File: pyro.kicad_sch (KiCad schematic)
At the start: 35 parts, among them J2 PYRO_1, J3 PYRO_2, J4 PYRO_3, J5 PYRO_4, Q0 BJT - NPN, Q1 PMOS, Q2 PMOS, Q3 PMOS, Q4 PMOS, Q5 NMOS, Q6 NMOS, Q7 NMOS, Q8 NMOS, Q9 NMOS

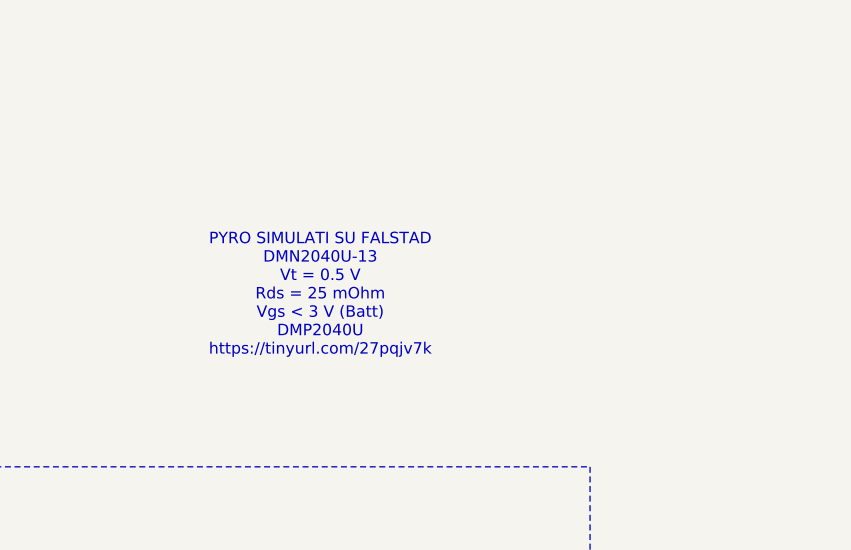
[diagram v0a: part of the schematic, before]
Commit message: update blocco pyro
scelta pmos e bjt
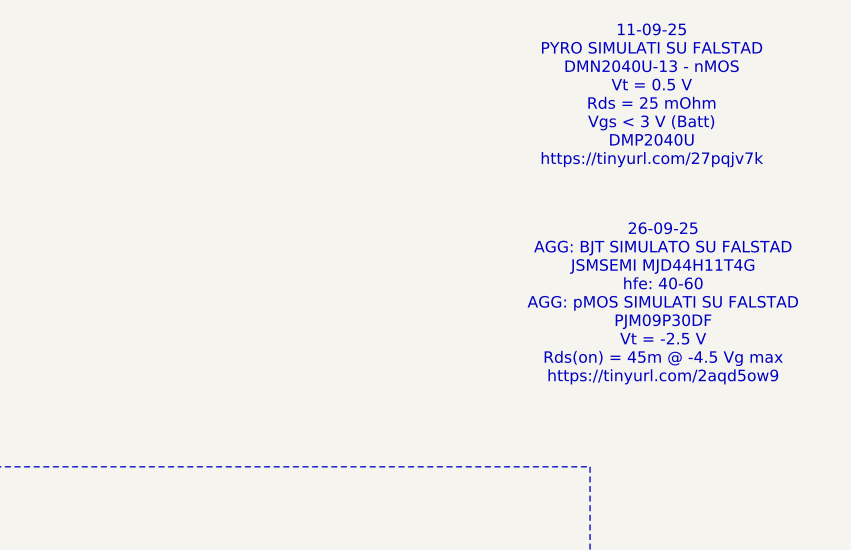
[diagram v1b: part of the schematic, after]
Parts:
- Q5, Q6, Q7, Q8, Q9: footprint (none) -> Package_TO_SOT_SMD:SOT-23_Handsoldering
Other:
- note added: "11-09-25 PYRO SIMULATI SU FALSTAD DMN2040U-13 - nMOS Vt = 0.5 V Rds = 25 mOhm Vgs < 3 V (Batt) DMP2040U https://tinyurl.com/27pqjv7k"
- note added: "26-09-25 AGG: BJT SIMULATO SU FALSTAD JSMSEMI MJD44H11T4G hfe: 40-60 AGG: pMOS SIMULATI SU FALSTAD PJM09P30DF Vt = -2.5 V Rds(on) = 45m @ -4.5 Vg max https://tinyurl.com/2aqd5ow9"
- note removed: "PYRO SIMULATI SU FALSTAD DMN2040U-13 Vt = 0.5 V Rds = 25 mOhm Vgs < 3 V (Batt) DMP2040U https://tinyurl.com/27pqjv7k"
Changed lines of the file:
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@@
 		)
 	)
-	(text "PYRO SIMULATI SU FALSTAD\nDMN2040U-13\nVt = 0.5 V\nRds = 25 mOhm\nVgs < 3 V (Batt)\nDMP2040U\nhttps://tinyurl.com/27pqjv7k"
+	(text "11-09-25\nPYRO SIMULATI SU FALSTAD\nDMN2040U-13 - nMOS\nVt = 0.5 V\nRds = 25 mOhm\nVgs < 3 V (Batt)\nDMP2040U\nhttps://tinyurl.com/27pqjv7k"
 		(exclude_from_sim no)
-		(at 217.678 45.72 0)
+		(at 254.508 23.622 0)
 		(effects
 			(font
@@
 		)
 	)
+	(text "26-09-25\nAGG: BJT SIMULATO SU FALSTAD\nJSMSEMI MJD44H11T4G\nhfe: 40-60\nAGG: pMOS SIMULATI SU FALSTAD\nPJM09P30DF\nVt = -2.5 V\nRds(on) = 45m @ -4.5 Vg max\nhttps://tinyurl.com/2aqd5ow9"
+		(exclude_from_sim no)
+		(at 255.778 46.736 0)
+		(effects
+			(font
+				(size 1.27 1.27)
+			)
+		)
+	)
 	(text "9"
 		(exclude_from_sim no)
@@
 			)
 		)
-		(property "Footprint" ""
+		(property "Footprint" "Package_TO_SOT_SMD:SOT-23_Handsoldering"
 			(at 76.2 88.9 0)
 			(effects
@@
 			)
 		)
-		(property "Footprint" ""
+		(property "Footprint" "Package_TO_SOT_SMD:SOT-23_Handsoldering"
 			(at 170.18 88.9 0)
 			(effects
@@
 			)
 		)
-		(property "Footprint" ""
+		(property "Footprint" "Package_TO_SOT_SMD:SOT-23_Handsoldering"
 			(at 123.19 88.9 0)
 			(effects
@@
 			)
 		)
-		(property "Footprint" ""
+		(property "Footprint" "Package_TO_SOT_SMD:SOT-23_Handsoldering"
 			(at 217.17 88.9 0)
 			(effects
@@
 			)
 		)
-		(property "Footprint" ""
+		(property "Footprint" "Package_TO_SOT_SMD:SOT-23_Handsoldering"
 			(at 151.13 135.89 0)
 			(effects

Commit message: bozza layout pcb
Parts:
- removed J2: PYRO_1, symbol Connector:Conn_01x02_Socket
- removed J3: PYRO_2, symbol Connector:Conn_01x02_Socket
- removed J4: PYRO_3, symbol Connector:Conn_01x02_Socket
- removed J5: PYRO_4, symbol Connector:Conn_01x02_Socket
- removed Q0: BJT - NPN, symbol Transistor_BJT:Q_NPN_BCE
- removed Q1, Q2, Q3, Q4: PMOS, symbol Simulation_SPICE:PMOS
- added J15: DB141R-2.54-8P-GN, DB141R-2-54-8:CONN16_DB141R_DIO, symbol 2025-09-27_12-32-40:DB141R-2.54-8P-GN
- added Q1: MJD44H11T4G, easyeda2kicad:TO-252-2_L6.5-W6.1-P4.58-LS10.0-TL, symbol WF5803F:MJD44H11T4G
- added Q10, Q11, Q12, Q13: PJM09P30DF, easyeda2kicad:DFN-6_L2.0-W2.0-P0.65-BL-EP-1, symbol WF5803F:PJM09P30DF
- added R9: 100, Resistor_SMD:R_0603_1608Metric_Pad0.98x0.95mm_HandSolder, symbol Device:R
- added U6: LT3092xST, Package_TO_SOT_SMD:SOT-223-3_TabPin2, symbol Reference_Current:LT3092xST
- R8: value 500 -> 200k
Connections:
- net +BATT: now also Q1.4 (C), U6.3; no longer R8.1
- net PYRO_HIGH: now also Q1.3 (E), Q10.4 (S), Q11.4 (S), Q12.4 (S), Q13.4 (S)
- net PYRO_LOW: now also J15.10, J15.12, J15.14, J15.16, J15.2, J15.4, J15.6, J15.8
- net at R15.2, R16.1: now also Q11.3 (G)
- net at R17.2, R34.1: now also Q12.3 (G)
- net at R12.2, R14.1: now also Q10.3 (G)
- net at R37.2, R38.1: now also Q13.3 (G)
- net at R8.2: now also Q1.1 (B), R9.2
- new net: R8.1, U6.1
- new net: R9.1, U6.2
- new net PYRO1: J15.1, J15.9, Q10.1 (D)
- new net PYRO2: J15.11, J15.3, Q11.1 (D)
- new net PYRO3: J15.13, J15.5, Q12.1 (D)
- new net PYRO4: J15.15, J15.7, Q13.1 (D)
- no-connect marks 0 -> 20
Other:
- note added: "27-09-25 AGG: GENERATORE DI CORRENTE LT3092 Iout = 20 mA Rout = 100 Ohm Rset = 200k Ohm https://tinyurl.com/2dp3mgog + aggiornamento beta pMOS beta = 2.27 https://tinyurl.com/2dp3mgog"

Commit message: led e buzzer
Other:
- moved on the sheet: J15
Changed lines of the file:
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@@
 	)
 	(junction
-		(at 78.74 173.99)
+		(at 64.77 153.67)
 		(diameter 0)
 		(color 0 0 0 0)
@@
 	)
 	(junction
-		(at 78.74 168.91)
+		(at 64.77 148.59)
 		(diameter 0)
 		(color 0 0 0 0)
@@
 	)
 	(junction
-		(at 78.74 179.07)
+		(at 64.77 158.75)
 		(diameter 0)
 		(color 0 0 0 0)
 	)
 	(junction
-		(at 78.74 158.75)
+		(at 64.77 138.43)
 		(diameter 0)
 		(color 0 0 0 0)
@@
 	)
 	(junction
-		(at 78.74 184.15)
+		(at 64.77 163.83)
 		(diameter 0)
 		(color 0 0 0 0)
 	)
 	(junction
-		(at 78.74 153.67)
+		(at 64.77 133.35)
 		(diameter 0)
 		(color 0 0 0 0)
@@
 	)
 	(junction
-		(at 78.74 148.59)
+		(at 64.77 128.27)
 		(diameter 0)
 		(color 0 0 0 0)
 	)
 	(junction
-		(at 78.74 163.83)
+		(at 64.77 143.51)
 		(diameter 0)
 		(color 0 0 0 0)
@@
 	(wire
 		(pts
-			(xy 78.74 173.99) (xy 78.74 176.53)
-		)
-		(stroke
-			(width 0)
-			(type default)
-		)
-	)
-	(wire
-		(pts
-			(xy 78.74 163.83) (xy 78.74 166.37)
+			(xy 64.77 153.67) (xy 64.77 156.21)
+		)
+		(stroke
+			(width 0)
+			(type default)
+		)
+	)
+	(wire
+		(pts
+			(xy 64.77 143.51) (xy 64.77 146.05)
 		)
 		(stroke
@@
 	(wire
 		(pts
-			(xy 78.74 148.59) (xy 78.74 151.13)
+			(xy 64.77 128.27) (xy 64.77 130.81)
 		)
 		(stroke
@@
 	(wire
 		(pts
-			(xy 78.74 184.15) (xy 78.74 186.69)
+			(xy 64.77 163.83) (xy 64.77 166.37)
 		)
 		(stroke
@@
 	(wire
 		(pts
-			(xy 68.58 153.67) (xy 78.74 153.67)
+			(xy 54.61 133.35) (xy 64.77 133.35)
 		)
 		(stroke
@@
 	(wire
 		(pts
-			(xy 68.58 173.99) (xy 78.74 173.99)
+			(xy 54.61 153.67) (xy 64.77 153.67)
 		)
 		(stroke
@@
 	(wire
 		(pts
-			(xy 78.74 153.67) (xy 78.74 156.21)
-		)
-		(stroke
-			(width 0)
-			(type default)
-		)
-	)
-	(wire
-		(pts
-			(xy 68.58 168.91) (xy 78.74 168.91)
+			(xy 64.77 133.35) (xy 64.77 135.89)
+		)
+		(stroke
+			(width 0)
+			(type default)
+		)
+	)
+	(wire
+		(pts
+			(xy 54.61 148.59) (xy 64.77 148.59)
 		)
 		(stroke
@@
 	(wire
 		(pts
-			(xy 78.74 158.75) (xy 78.74 161.29)
+			(xy 64.77 138.43) (xy 64.77 140.97)
 		)
 		(stroke
@@
 	(wire
 		(pts
-			(xy 68.58 158.75) (xy 78.74 158.75)
-		)
-		(stroke
-			(width 0)
-			(type default)
-		)
-	)
-	(wire
-		(pts
-			(xy 68.58 163.83) (xy 78.74 163.83)
+			(xy 54.61 138.43) (xy 64.77 138.43)
+		)
+		(stroke
+			(width 0)
+			(type default)
+		)
+	)
+	(wire
+		(pts
+			(xy 54.61 143.51) (xy 64.77 143.51)
 		)
 		(stroke
@@
 	(wire
 		(pts
-			(xy 68.58 184.15) (xy 78.74 184.15)
+			(xy 54.61 163.83) (xy 64.77 163.83)
 		)
 		(stroke
@@
 	(wire
 		(pts
-			(xy 68.58 179.07) (xy 78.74 179.07)
+			(xy 54.61 158.75) (xy 64.77 158.75)
 		)
 		(stroke
@@
 	(wire
 		(pts
-			(xy 78.74 179.07) (xy 78.74 181.61)
+			(xy 64.77 158.75) (xy 64.77 161.29)
 		)
 		(stroke
@@
 	(wire
 		(pts
-			(xy 68.58 148.59) (xy 78.74 148.59)
-		)
-		(stroke
-			(width 0)
-			(type default)
-		)
-	)
-	(wire
-		(pts
-			(xy 78.74 168.91) (xy 78.74 171.45)
+			(xy 54.61 128.27) (xy 64.77 128.27)
+		)
+		(stroke
+			(width 0)
+			(type default)
+		)
+	)
+	(wire
+		(pts
+			(xy 64.77 148.59) (xy 64.77 151.13)
 		)
 		(stroke
@@
 	)
 	(label "PYRO_LOW"
-		(at 68.58 173.99 180)
+		(at 54.61 153.67 180)
 		(effects
 			(font
@@
 	)
 	(label "PYRO_LOW"
-		(at 68.58 163.83 180)
+		(at 54.61 143.51 180)
 		(effects
 			(font
@@
 	)
 	(label "PYRO2"
-		(at 68.58 158.75 180)
+		(at 54.61 138.43 180)
 		(effects
 			(font
@@
 	)
 	(label "PYRO3"
-		(at 68.58 168.91 180)
+		(at 54.61 148.59 180)
 		(effects
 			(font
@@
 	)
 	(label "PYRO4"
-		(at 68.58 179.07 180)
+		(at 54.61 158.75 180)
 		(effects
 			(font
@@
 	)
 	(label "PYRO_LOW"
-		(at 68.58 184.15 180)
+		(at 54.61 163.83 180)
 		(effects
 			(font
@@
 	)
 	(label "PYRO_LOW"
-		(at 68.58 153.67 180)
+		(at 54.61 133.35 180)
 		(effects
 			(font
@@
 	)
 	(label "PYRO1"
-		(at 68.58 148.59 180)
+		(at 54.61 128.27 180)
 		(effects
 			(font
@@
 	(symbol
 		(lib_id "2025-09-27_12-32-40:DB141R-2.54-8P-GN")
-		(at 78.74 148.59 0)
+		(at 64.77 128.27 0)
 		(unit 1)
 		(exclude_from_sim no)
@@
 		(fields_autoplaced yes)
 		(property "Reference" "J15"
-			(at 92.71 166.3699 0)
+			(at 78.74 146.0499 0)
 			(effects
 				(font
@@
 		)
 		(property "Value" "DB141R-2.54-8P-GN"
-			(at 92.71 168.9099 0)
+			(at 78.74 148.5899 0)
 			(effects
 				(font
@@
 		)
 		(property "Footprint" "DB141R-2-54-8:CONN16_DB141R_DIO"
-			(at 78.74 148.59 0)
+			(at 64.77 128.27 0)
 			(effects
 				(font
@@
 		)
 		(property "Datasheet" "DB141R-2.54-8P-GN"
-			(at 78.74 148.59 0)
+			(at 64.77 128.27 0)
 			(effects
 				(font
@@
 		)
 		(property "Description" ""
-			(at 78.74 148.59 0)
-			(effects
-				(font
+			(at 64.77 128.27 0)
+			(effects
+				(font

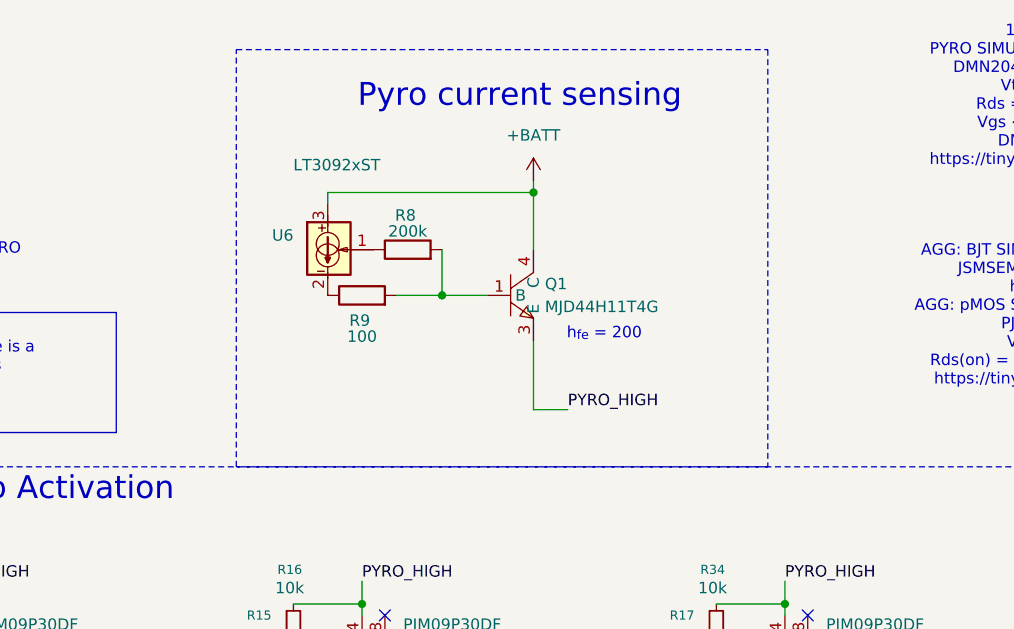
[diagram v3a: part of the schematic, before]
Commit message: Small changes
modified Main LEDs.
Added Radio LEDs.

Connected the GPS uart to the Radio.
Added a test point for the GPS PRG pin.

Modified the Pyro current limiter for better BOM compliance.

Modified a copule of estetic things on the schematic.
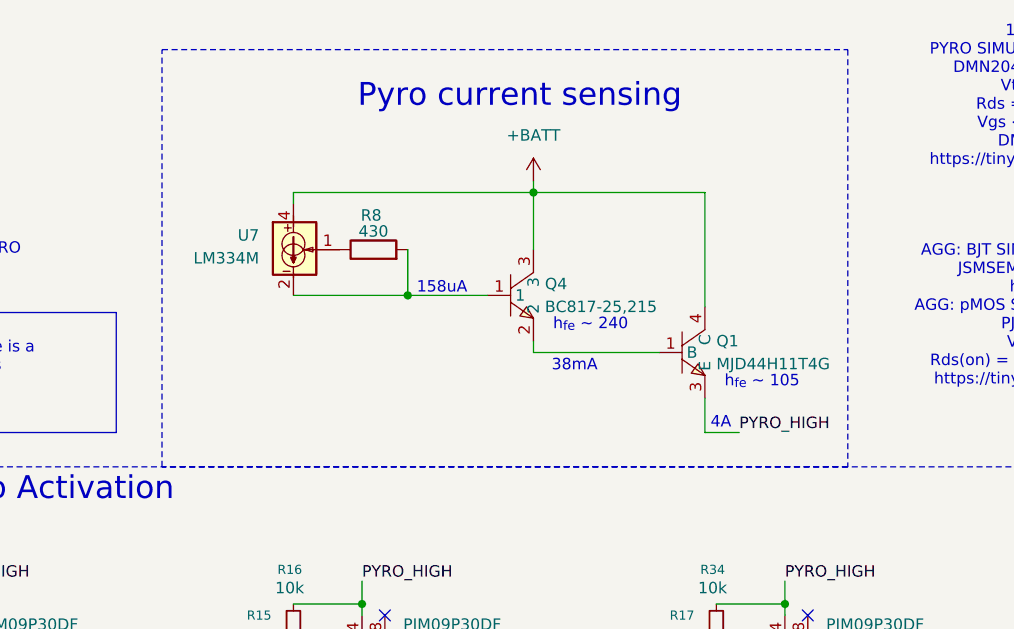
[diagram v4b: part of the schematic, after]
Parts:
- removed R9: 100, Resistor_SMD:R_0603_1608Metric_Pad0.98x0.95mm_HandSolder, symbol Device:R
- removed U6: LT3092xST, Package_TO_SOT_SMD:SOT-223-3_TabPin2, symbol Reference_Current:LT3092xST
- added Q4: BC817-25,215, BC817-25:SOT-23-3_L2.9-W1.6-P1.90-LS2.8-BR, symbol BC817-25:BC817-25,215
- added U7: LM334M, Package_SO:SOIC-8_3.9x4.9mm_P1.27mm, symbol Reference_Current:LM334M
- R8: value 200k -> 430
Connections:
- net +BATT: now also Q4.3, U7.4
- net at R8.1: now also U7.1
- net at R8.2: now also Q4.1, U7.2, U7.3, U7.6, U7.7; no longer Q1.1 (B)
- new net: Q1.1 (B), Q4.2
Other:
- note added: "158uA"
- note added: "38mA"
- note added: "4A"
- note added: "h_{fe} ~ 105"
- note added: "h_{fe} ~ 240"
- note removed: "h_{fe} = 200"
- moved on the sheet: Q1, R8
